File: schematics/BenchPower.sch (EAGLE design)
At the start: 23 parts, among them U1 V_REG_317SINK, U2 V_REG_317SINK, X2 9090-4R

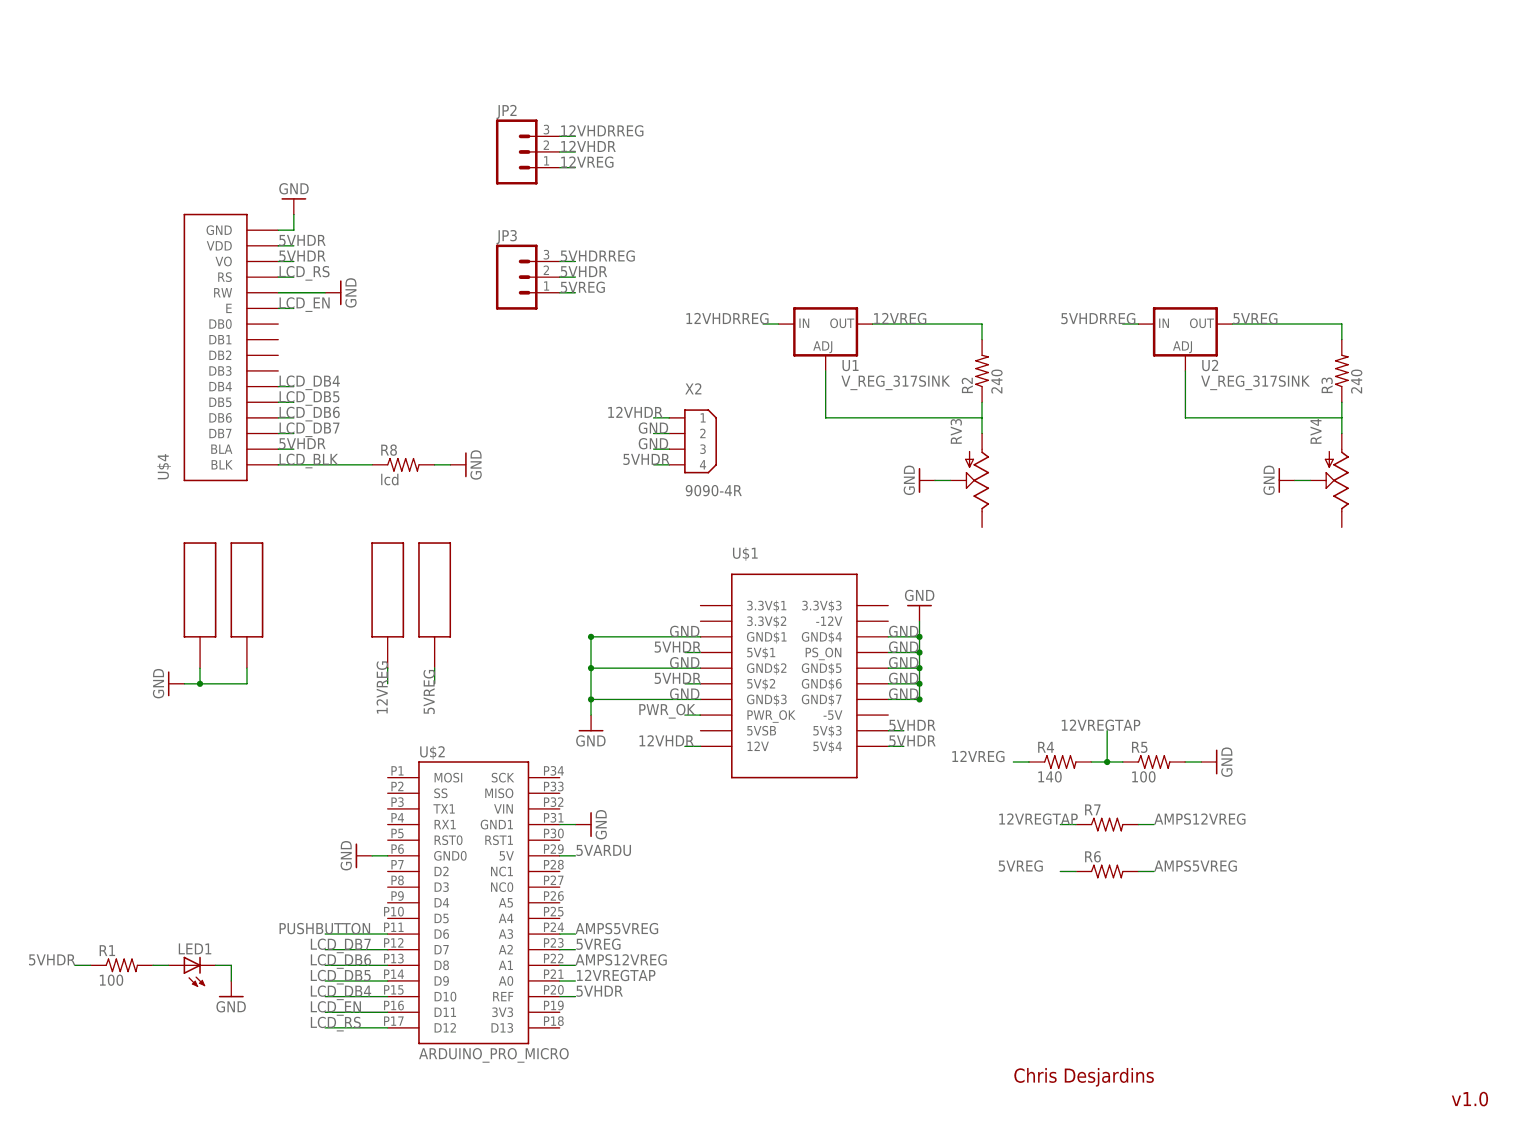
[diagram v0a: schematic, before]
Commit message: Updates to bench power
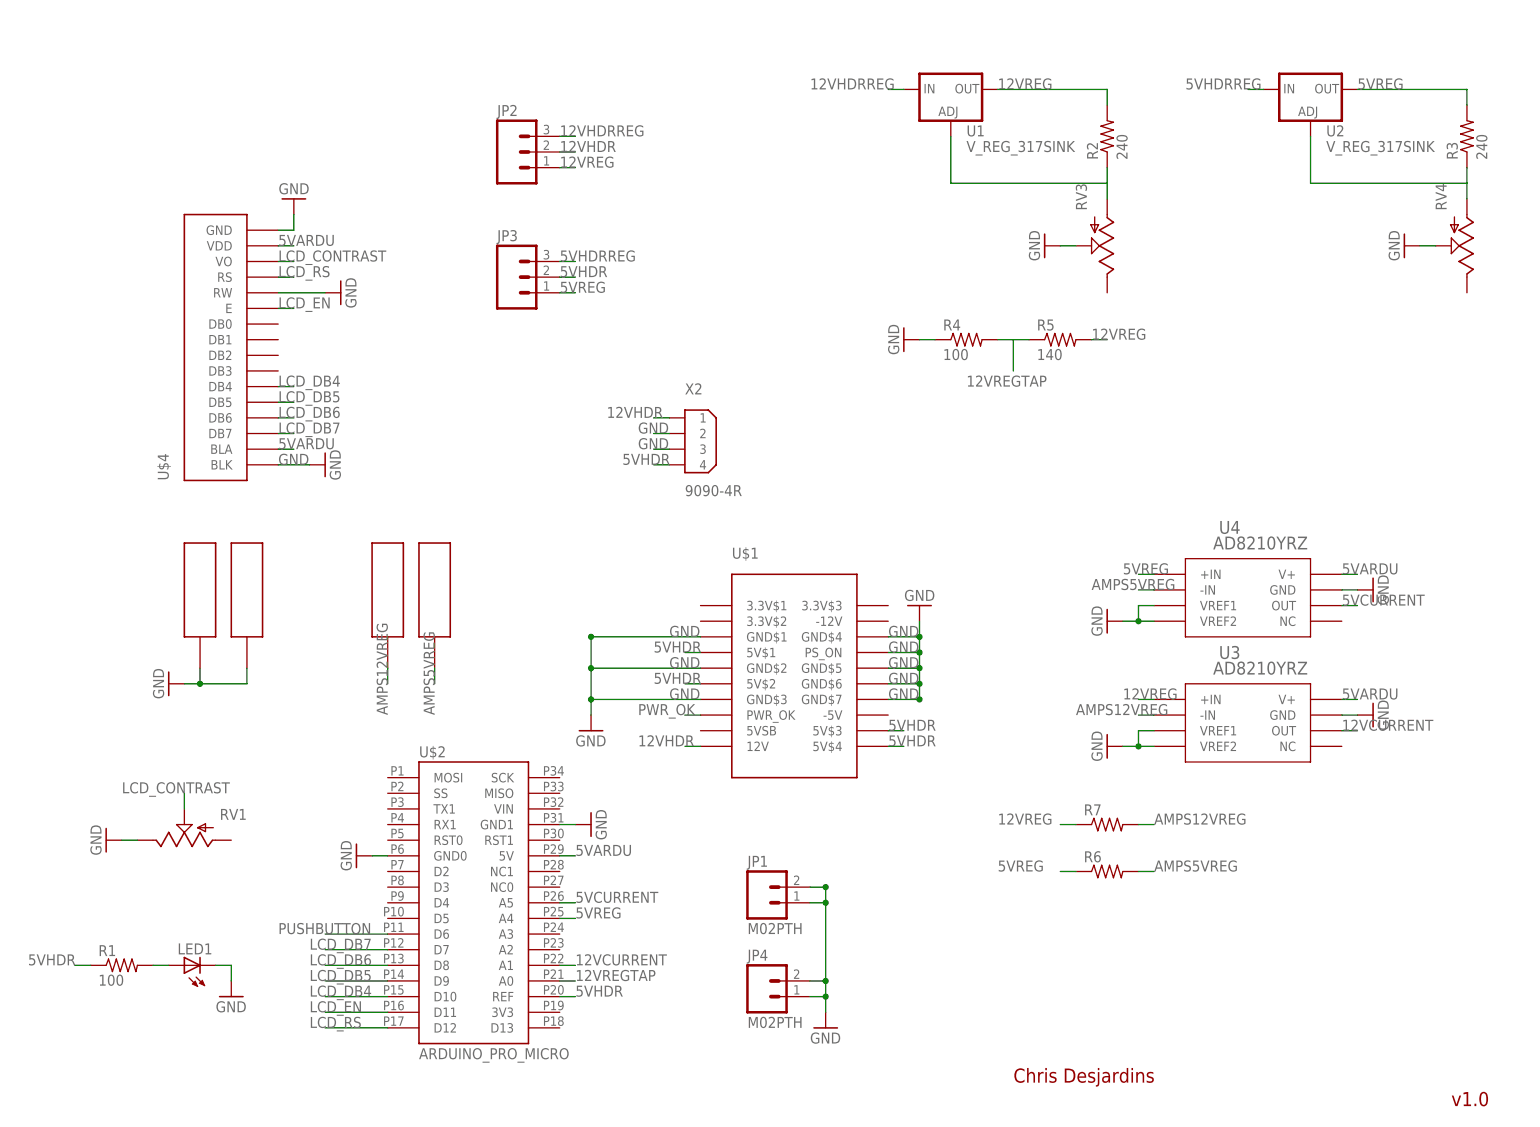
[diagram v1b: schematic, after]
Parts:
- removed R8: lcd, SparkFun-Passives:RESISTORAXIAL-0.3
- added JP1, JP4: M02PTH, SparkFun-Connectors:M02PTH
- added RV1: (no value), desjardins:POT3266
- added U3, U4: AD8210YRZ, desjardins:AD8210YRZ
- R4: value 140 -> 100; device SparkFun-Resistors:RESISTORAXIAL-0.3 -> SparkFun-Passives:RESISTORAXIAL-0.3
- R5: value 100 -> 140; device SparkFun-Resistors:RESISTORAXIAL-0.3 -> SparkFun-Passives:RESISTORAXIAL-0.3
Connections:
- removed net LCD_BLK: R8.1, U$4.BLK
- new net 12VCURRENT: U$2.A1, U3.OUT
- new net 5VCURRENT: U$2.A5, U4.OUT
- new net LCD_CONTRAST: RV1.S, U$4.VO
- net 12VREG: now also R5.2, R7.1, U3.+IN; no longer PWR1.P$1, R4.1
- net 12VREGTAP: no longer R7.1
- net 5VARDU: now also U$4.BLA, U$4.VDD, U3.V+, U4.V+
- net 5VHDR: no longer U$4.BLA, U$4.VDD, U$4.VO
- net 5VREG: now also U$2.A4, U4.+IN; no longer PWR2.P$1, U$2.A2
- net AMPS12VREG: now also PWR1.P$1, U3.-IN; no longer U$2.A1
- net AMPS5VREG: now also PWR2.P$1, U4.-IN; no longer U$2.A3
- net GND: now also JP1.1, JP1.2, JP4.1, JP4.2, R4.1, RV1.E, U$4.BLK, U3.GND, U3.VREF1, U3.VREF2, U4.GND, U4.VREF1, U4.VREF2; no longer R5.2, R8.2
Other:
- moved on the sheet: R2, R3, R4, R5, RV3, RV4, U1, U2

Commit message: Use new op amp
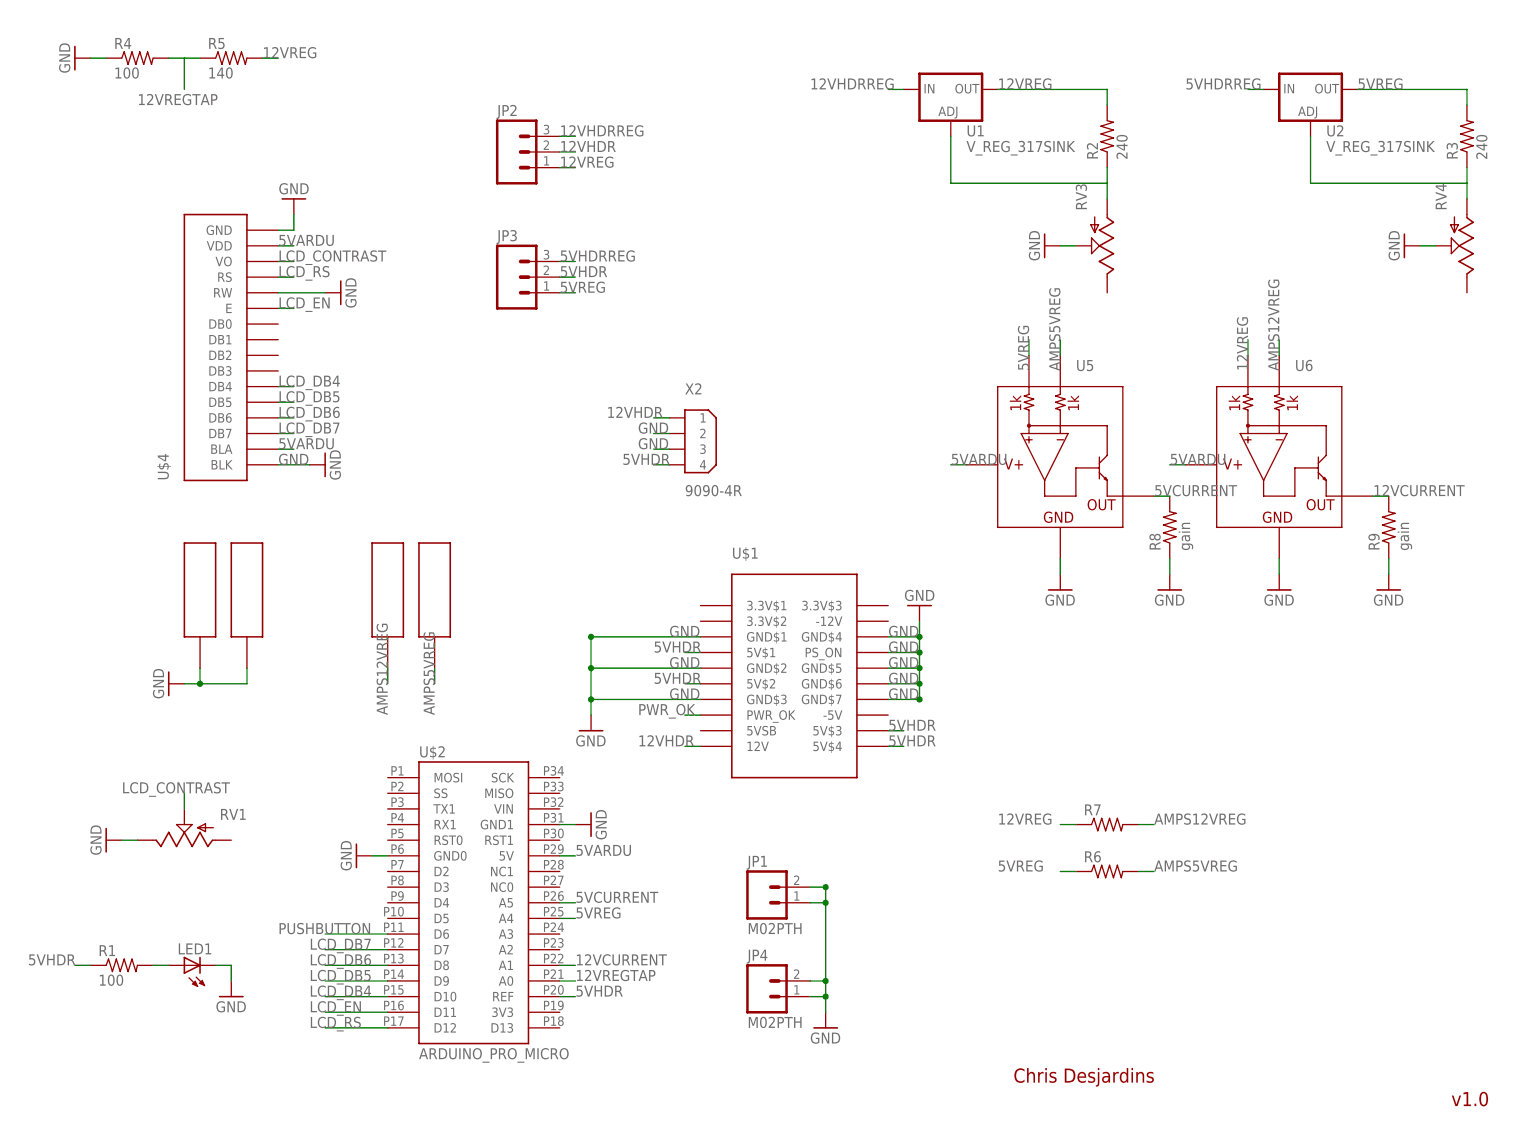
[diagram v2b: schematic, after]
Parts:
- removed U3, U4: AD8210YRZ, desjardins:AD8210YRZ
- added R8, R9: gain, SparkFun-Passives:RESISTORAXIAL-0.3
- added U5, U6: (no value), SparkFun-AnalogIC:INA139
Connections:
- net 12VCURRENT: now also R9.2, U6.OUT; no longer U3.OUT
- net 12VREG: now also U6.VIN+; no longer U3.+IN
- net 5VARDU: now also U5.V+, U6.V+; no longer U3.V+, U4.V+
- net 5VCURRENT: now also R8.2, U5.OUT; no longer U4.OUT
- net 5VREG: now also U5.VIN+; no longer U4.+IN
- net AMPS12VREG: now also U6.VIN-; no longer U3.-IN
- net AMPS5VREG: now also U5.VIN-; no longer U4.-IN
- net GND: now also R8.1, R9.1, U5.GND, U6.GND; no longer U3.GND, U3.VREF1, U3.VREF2, U4.GND, U4.VREF1, U4.VREF2
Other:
- moved on the sheet: R4, R5

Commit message: Simplify
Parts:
- removed JP2, JP3: (no value), SparkFun-Connectors:M03PTH
- removed RV4: (no value), desjardins:POT
- removed U2: V_REG_317SINK, SparkFun-PowerIC:V_REG_317SINK
- added R10: 140, SparkFun-Passives:RESISTORAXIAL-0.3
- added S1: EG1213, adafruit:EG1213
- R3: value 240 -> 100
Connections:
- net 12VCURRENT renamed 12VREGCURRENT
- net 5VCURRENT renamed 12VHDRCURRENT
- net AMPS5VREG renamed AMPS12VHDR
- removed net 12VHDRREG: JP2.3, U1.IN
- removed net 5VHDRREG: JP3.3, U2.IN
- removed net 5VREG: JP3.1, R3.2, R6.1, U$2.A4, U2.OUT, U5.VIN+
- removed net ADJREG2: R3.1, RV4.A, U2.ADJ
- removed net PUSHBUTTON: U$2.D6
- new net 12VHDRSW: R10.2, R6.1, S11.P, U1.IN, U5.VIN+
- new net 12VHDRTAP: R10.1, R3.2, U$2.A4
- net 12VHDR: now also S11.O, U$2.VIN; no longer JP2.2
- net 12VREG: no longer JP2.1
- net 5VHDR: no longer JP3.2
- net GND: now also R3.1; no longer RV4.S
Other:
- moved on the sheet: R3, R8, R9, U5, U6

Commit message: Final pass
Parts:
- removed S1: EG1213, adafruit:EG1213
- added S2: EG1213, desjardins:EG1213
- R1: value 100 -> 1000
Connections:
- net 12VHDR: now also S2.O; no longer S11.O
- net 12VHDRSW: now also R1.1, S2.P; no longer S11.P
- net 5VHDR: no longer R1.1
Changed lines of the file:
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@@
 <part name="U$2" library="ChrisD" deviceset="ARDUINO_PRO_MICRO" device=""/>
 <part name="U1" library="SparkFun-PowerIC" deviceset="V_REG_317" device="SINK"/>
-<part name="R1" library="SparkFun-Passives" deviceset="RESISTOR" device="AXIAL-0.3" value="100"/>
+<part name="R1" library="SparkFun-Passives" deviceset="RESISTOR" device="AXIAL-0.3" value="1000"/>
 <part name="GND2" library="SparkFun-Aesthetics" deviceset="GND" device=""/>
 <part name="R2" library="SparkFun-Passives" deviceset="RESISTOR" device="AXIAL-0.3" value="240"/>
@@
 <part name="R10" library="SparkFun-Passives" deviceset="RESISTOR" device="AXIAL-0.3" value="140"/>
 <part name="GND3" library="SparkFun-Aesthetics" deviceset="GND" device=""/>
-<part name="S1" library="adafruit" deviceset="EG1213" device=""/>
+<part name="S2" library="desjardins" deviceset="EG1213" device=""/>
 </parts>
 <sheets>
@@
 <instance part="R10" gate="G$1" x="86.36" y="177.8"/>
 <instance part="GND3" gate="1" x="60.96" y="177.8" rot="R270"/>
-<instance part="S1" gate="1" x="15.24" y="96.52"/>
+<instance part="S2" gate="1" x="17.78" y="121.92"/>
 </instances>
 <busses>
@@
 <label x="93.98" y="25.4" size="1.778" layer="95"/>
 </segment>
-<segment>
-<pinref part="R1" gate="G$1" pin="1"/>
-<wire x1="15.24" y1="30.48" x2="12.7" y2="30.48" width="0.1524" layer="91"/>
-<label x="5.08" y="30.48" size="1.778" layer="95"/>
-</segment>
 </net>
 <net name="12VHDR" class="0">
@@
 </segment>
 <segment>
-<pinref part="S1" gate="1" pin="O"/>
-<wire x1="12.7" y1="101.6" x2="12.7" y2="104.14" width="0.1524" layer="91"/>
-<label x="12.7" y="104.14" size="1.778" layer="95"/>
+<pinref part="S2" gate="1" pin="O"/>
+<wire x1="15.24" y1="127" x2="15.24" y2="129.54" width="0.1524" layer="91"/>
 </segment>
 </net>
@@
 </segment>
 <segment>
-<pinref part="S1" gate="1" pin="P"/>
-<wire x1="15.24" y1="91.44" x2="15.24" y2="88.9" width="0.1524" layer="91"/>
-<label x="10.16" y="86.36" size="1.778" layer="95"/>
-</segment>
-</net>
+<pinref part="S2" gate="1" pin="P"/>
+<wire x1="17.78" y1="116.84" x2="17.78" y2="114.3" width="0.1524" layer="91"/>
+</segment>
+<segment>
+<pinref part="R1" gate="G$1" pin="1"/>
+<wire x1="15.24" y1="30.48" x2="12.7" y2="30.48" width="0.1524" layer="91"/>
+<label x="2.54" y="30.48" size="1.778" layer="95"/>
+</segment>
+</net>

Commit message: Updates for rev 2
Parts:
- removed R10: 140, SparkFun-Passives:RESISTORAXIAL-0.3
- removed R3: 100, SparkFun-Passives:RESISTORAXIAL-0.3
- removed U$6: BINDINGPOST, desjardins:BINDINGPOST
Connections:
- net 12VHDRSW: no longer R10.2
- net 12VHDRTAP: no longer R10.1, R3.2
- net GND: no longer R3.1, U$6.P$1
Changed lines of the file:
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@@
 <part name="FRAME1" library="ChrisD" deviceset="FRAME-LETTER" device=""/>
 <part name="U$5" library="desjardins" deviceset="BINDINGPOST" device=""/>
-<part name="U$6" library="desjardins" deviceset="BINDINGPOST" device=""/>
 <part name="GND1" library="SparkFun-Aesthetics" deviceset="GND" device=""/>
 <part name="X2" library="con-thomas-betts" deviceset="9090-4" device="R"/>
@@
 <part name="GND5" library="SparkFun-Aesthetics" deviceset="GND" device=""/>
 <part name="GND13" library="SparkFun-Aesthetics" deviceset="GND" device=""/>
-<part name="R3" library="SparkFun-Passives" deviceset="RESISTOR" device="AXIAL-0.3" value="100"/>
-<part name="R10" library="SparkFun-Passives" deviceset="RESISTOR" device="AXIAL-0.3" value="140"/>
-<part name="GND3" library="SparkFun-Aesthetics" deviceset="GND" device=""/>
 <part name="S2" library="desjardins" deviceset="EG1213" device=""/>
 </parts>
@@
 <instance part="FRAME1" gate="G$2" x="147.32" y="0"/>
 <instance part="U$5" gate="G$1" x="33.02" y="91.44"/>
-<instance part="U$6" gate="G$1" x="40.64" y="91.44"/>
-<instance part="GND1" gate="1" x="27.94" y="76.2" rot="R270"/>
+<instance part="GND1" gate="1" x="33.02" y="73.66"/>
 <instance part="X2" gate="G$1" x="111.76" y="114.3"/>
 <instance part="U$1" gate="G$1" x="129.54" y="76.2"/>
@@
 <instance part="GND5" gate="1" x="228.6" y="71.12"/>
 <instance part="GND13" gate="1" x="228.6" y="132.08"/>
-<instance part="R3" gate="G$1" x="71.12" y="177.8"/>
-<instance part="R10" gate="G$1" x="86.36" y="177.8"/>
-<instance part="GND3" gate="1" x="60.96" y="177.8" rot="R270"/>
 <instance part="S2" gate="1" x="17.78" y="121.92"/>
 </instances>
@@
 <net name="GND" class="0">
 <segment>
-<wire x1="40.64" y1="76.2" x2="33.02" y2="76.2" width="0.1524" layer="91"/>
-<wire x1="33.02" y1="76.2" x2="30.48" y2="76.2" width="0.1524" layer="91"/>
-<pinref part="U$6" gate="G$1" pin="P$1"/>
-<wire x1="40.64" y1="78.74" x2="40.64" y2="76.2" width="0.1524" layer="91"/>
 <pinref part="U$5" gate="G$1" pin="P$1"/>
 <wire x1="33.02" y1="78.74" x2="33.02" y2="76.2" width="0.1524" layer="91"/>
-<junction x="33.02" y="76.2"/>
 <pinref part="GND1" gate="1" pin="GND"/>
 </segment>
@@
 <pinref part="GND13" gate="1" pin="GND"/>
 </segment>
-<segment>
-<pinref part="R3" gate="G$1" pin="1"/>
-<wire x1="66.04" y1="177.8" x2="63.5" y2="177.8" width="0.1524" layer="91"/>
-<pinref part="GND3" gate="1" pin="GND"/>
-</segment>
 </net>
 <net name="5VHDR" class="0">
@@
 <net name="12VHDRTAP" class="0">
 <segment>
-<pinref part="R3" gate="G$1" pin="2"/>
-<wire x1="76.2" y1="177.8" x2="78.74" y2="177.8" width="0.1524" layer="91"/>
-<pinref part="R10" gate="G$1" pin="1"/>
-<wire x1="78.74" y1="177.8" x2="81.28" y2="177.8" width="0.1524" layer="91"/>
-<wire x1="78.74" y1="177.8" x2="78.74" y2="172.72" width="0.1524" layer="91"/>
-<label x="71.12" y="170.18" size="1.778" layer="95"/>
-</segment>
-<segment>
 <pinref part="U$2" gate="G$1" pin="A4"/>
 <wire x1="91.44" y1="38.1" x2="93.98" y2="38.1" width="0.1524" layer="91"/>
@@
 </segment>
 <segment>
-<pinref part="R10" gate="G$1" pin="2"/>
-<wire x1="91.44" y1="177.8" x2="93.98" y2="177.8" width="0.1524" layer="91"/>
-<label x="91.44" y="177.8" size="1.778" layer="95"/>
-</segment>
-<segment>
